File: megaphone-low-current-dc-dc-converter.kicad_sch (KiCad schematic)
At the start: 53 parts, among them Q1 SI7272DP, Q3 2N7002, U2 AP63203WU, U3 ACS712, U4 ACS712, U5 MCP4018

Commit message: change all MPPT references in files to new project name
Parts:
- L1: footprint MPPT Charge Controller Footprint Library:L_Vishay_6.9x6.5 -> megaphone-low-current-dc-dc-converter Footprint Library:L_Vishay_6.9x6.5
- U1: footprint MPPT Charge Controller Footprint Library:VQFN-16_EP_3.5x3.5_Pitch0.5mm -> megaphone-low-current-dc-dc-converter Footprint Library:VQFN-16_EP_3.5x3.5_Pitch0.5mm; symbol MPPT Charge Controller Symbol Library:BQ24650 -> megaphone-low-current-dc-dc-converter Symbol Library:BQ24650
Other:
- title: MEGAphone MPPT Charge Controller -> MEGAphone megaphone-low-current-dc-dc-converter

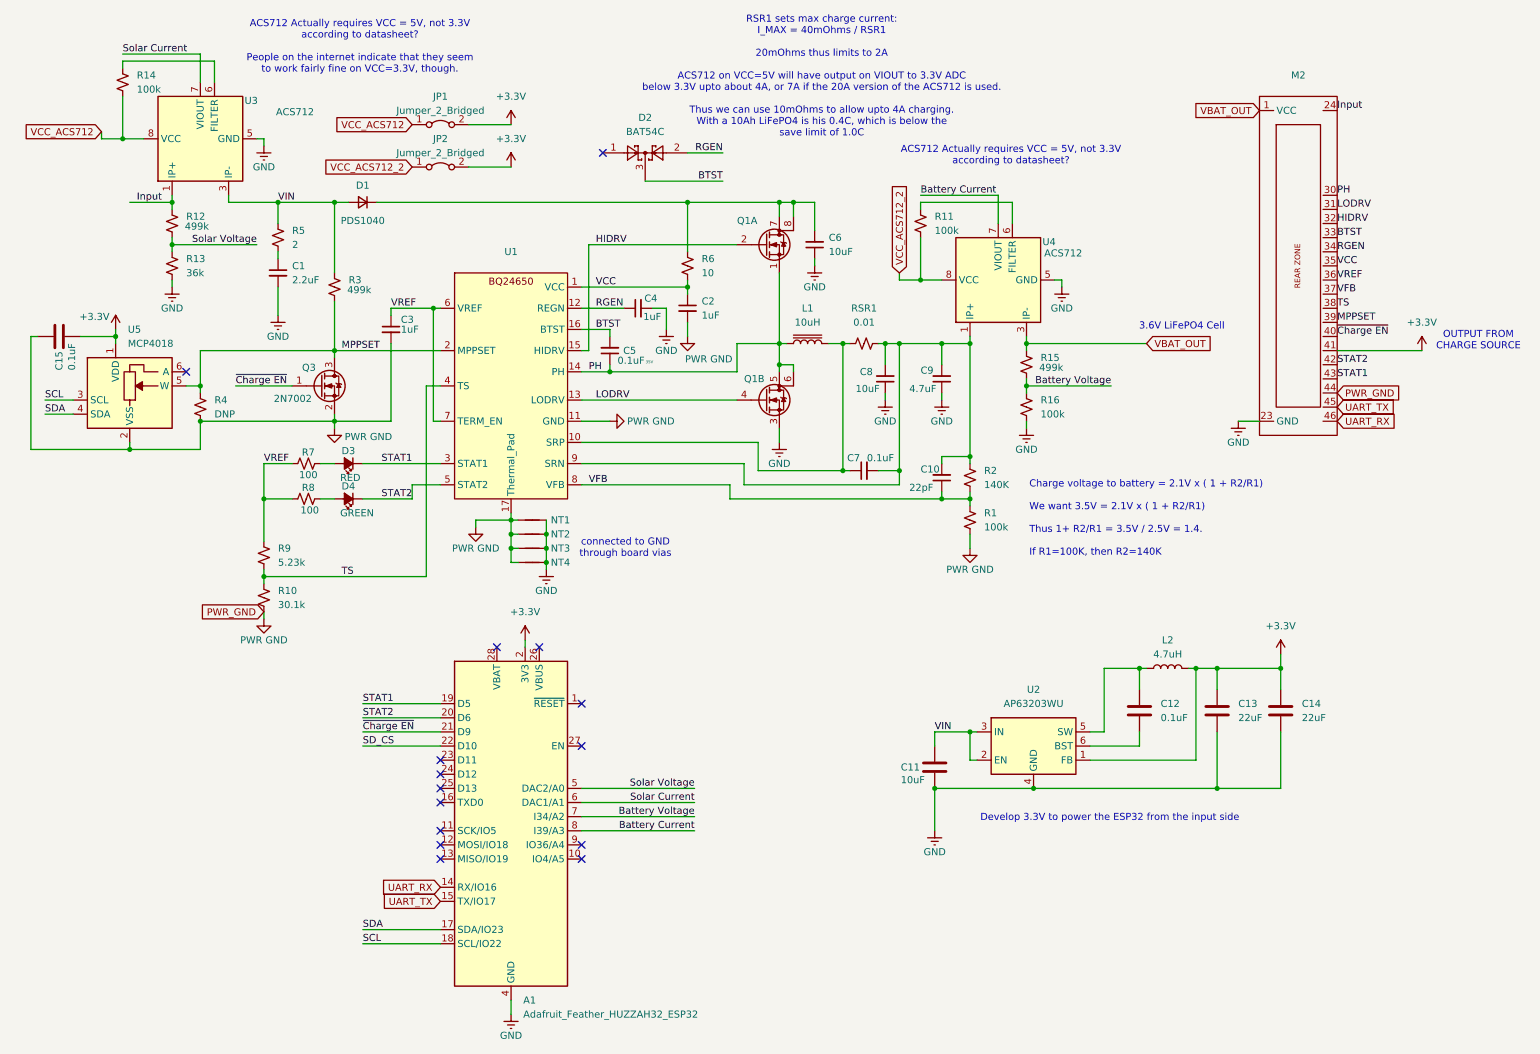
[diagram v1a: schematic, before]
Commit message: prune out unnecessary part of schematic
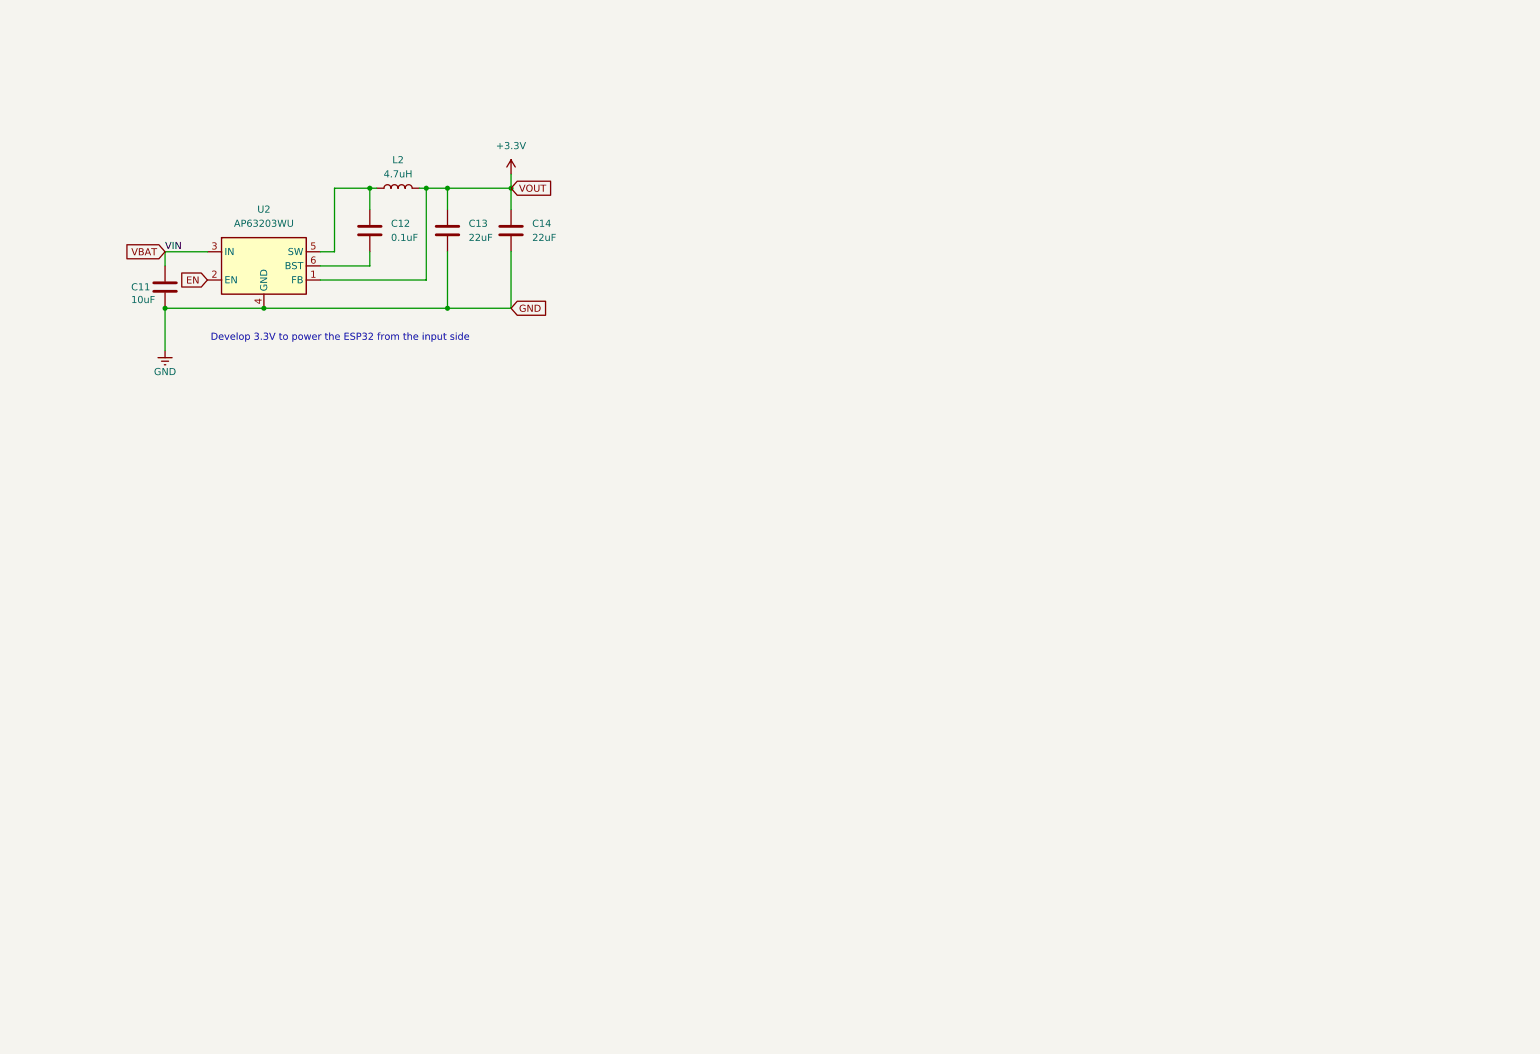
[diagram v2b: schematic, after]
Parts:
- removed A1: Adafruit_Feather_HUZZAH32_ESP32, Module:Adafruit_Feather, symbol MCU_Module:Adafruit_Feather_HUZZAH32_ESP32
- removed C1: 2.2uF, Capacitor_SMD:C_1210_3225Metric, symbol Device:C_Small
- removed C10: 22pF, Capacitor_SMD:C_0603_1608Metric, symbol Device:C_Small
- removed C15: 0.1uF, Capacitor_SMD:C_0603_1608Metric, symbol Device:C
- removed C2, C3, C4: 1uF, Capacitor_SMD:C_0603_1608Metric, symbol Device:C_Small
- removed C5, C7: 0.1uF, Capacitor_SMD:C_0603_1608Metric, symbol Device:C_Small
- removed C6, C8: 10uF, Capacitor_SMD:C_1206_3216Metric, symbol Device:C_Small
- removed C9: 4.7uF, Capacitor_SMD:C_0805_2012Metric, symbol Device:C_Small
- removed D1: PDS1040, Diode_SMD:D_PowerDI-5, symbol Device:D_Small
- removed D2: BAT54C, Package_TO_SOT_SMD:SOT-23, symbol Diode:BAT54C
- removed D3: RED, LED_SMD:LED_0603_1608Metric, symbol Device:LED_Small_Filled
- removed D4: GREEN, LED_SMD:LED_0603_1608Metric, symbol Device:LED_Small_Filled
- removed JP1, JP2: Jumper_2_Bridged, Jumper:SolderJumper-2_P1.3mm_Bridged_RoundedPad1.0x1.5mm, symbol Jumper:Jumper_2_Bridged
- removed L1: 10uH, megaphone-low-current-dc-dc-converter Footprint Library:L_Vishay_6.9x6.5, symbol Device:L_Iron
- removed M2: ~, MegaCastle:MegaCastle2x23-Module-I30.0x53.6-M80000307FFFC-PANEL, symbol MegaCastle:MegaCastle2x23-Module-I30.0x53.6-M80000307FFFC
- removed NT1, NT2, NT3, NT4: ~, NetTie:NetTie-2_SMD_Pad0.5mm, symbol Device:NetTie_2
- removed Q1: SI7272DP, Package_SO:PowerPAK_SO-8_Dual, symbol Device:Q_Dual_NMOS_S1G1S2G2D2D2D1D1
- removed Q3: 2N7002, Package_TO_SOT_SMD:SOT-23, symbol Transistor_FET:2N7002
- removed R1, R11, R14, R16: 100k, Resistor_SMD:R_0603_1608Metric, symbol Device:R_Small_US
- removed R10: 30.1k, Resistor_SMD:R_0603_1608Metric, symbol Device:R_Small_US
- removed R12, R15, R3: 499k, Resistor_SMD:R_0603_1608Metric, symbol Device:R_Small_US
- removed R13: 36k, Resistor_SMD:R_0603_1608Metric, symbol Device:R_Small_US
- removed R2: 140K, Resistor_SMD:R_0603_1608Metric, symbol Device:R_Small_US
- removed R4: DNP, Resistor_SMD:R_0603_1608Metric, symbol Device:R_Small_US
- removed R5: 2, Resistor_SMD:R_2512_6332Metric, symbol Device:R_Small_US
- removed R6: 10, Resistor_SMD:R_0603_1608Metric, symbol Device:R_Small_US
- removed R7, R8: 100, Resistor_SMD:R_0603_1608Metric, symbol Device:R_Small_US
- removed R9: 5.23k, Resistor_SMD:R_0603_1608Metric, symbol Device:R_Small_US
- removed RSR1: 0.01, Resistor_SMD:R_1206_3216Metric, symbol Device:R_Small_US
- removed U1: ~, megaphone-low-current-dc-dc-converter Footprint Library:VQFN-16_EP_3.5x3.5_Pitch0.5mm, symbol megaphone-low-current-dc-dc-converter Symbol Library:BQ24650
- removed U3, U4: ACS712, Package_SO:SOIC-8_3.9x4.9mm_P1.27mm, symbol Sensor_Current:ACS712xLCTR-05B
- removed U5: MCP4018, Package_TO_SOT_SMD:SOT-363_SC-70-6, symbol Potentiometer_Digital:MCP4018-xxxxLT
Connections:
- net VIN renamed VBAT
- net VBAT: no longer U2.2 (EN)
- new net EN: U2.2 (EN)
- no-connect marks 15 -> 0
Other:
- note removed: "3.6V LiFePO4 Cell"
- note removed: "ACS712 Actually requires VCC = 5V, not 3.3V according to datasheet?"
- note removed: "ACS712 Actually requires VCC = 5V, not 3.3V according to datasheet? People on the internet indicate that they seem to work fairly fine on VCC=3.3V, though."
- note removed: "Charge voltage to battery = 2.1V x ( 1 + R2/R1) We want 3.5V = 2.1V x ( 1 + R2/R1) Thus 1+ R2/R1 = 3.5V / 2.5V = 1.4. If R1=100K, then R2=140K"
- note removed: "OUTPUT FROM CHARGE SOURCE"
- note removed: "RSR1 sets max charge current: I_MAX = 40mOhms / RSR1 20mOhms thus limits to 2A ACS712 on VCC=5V will have output on VIOUT to 3.3V ADC below 3.3V upto about 4A, or 7A if the 20A version of the ACS712 is used. Thus we can use 10mOhms to allow upto 4A charging. With a 10Ah LiFePO4 is his 0.4C, which is below the save limit of 1.0C"
- note removed: "connected to GND through board vias"
- moved on the sheet: C11, C12, C13, C14, L2, U2

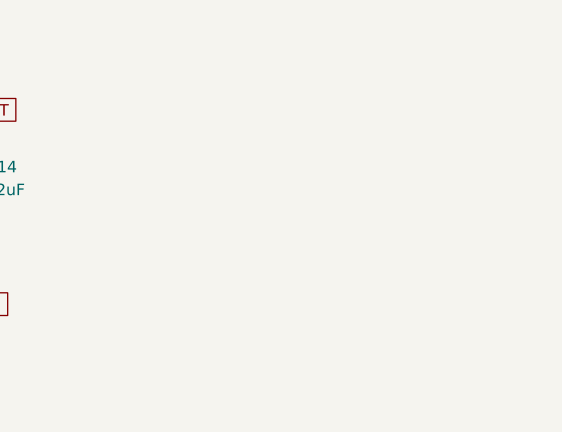
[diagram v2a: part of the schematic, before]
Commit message: finish adapting MPPT into simple low-current 3.3V DC:DC regulator
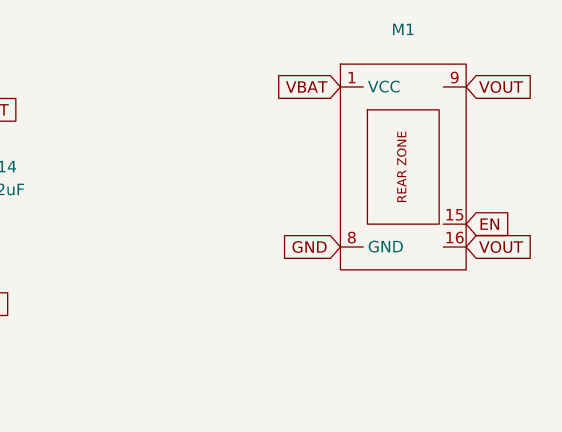
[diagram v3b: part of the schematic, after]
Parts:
- added M1: ~, MegaCastle:MegaCastle2x8-Module-I7.0x15.5-M8183, symbol MegaCastle:MegaCastle2x8-Module-I7.0x15.5-M8183
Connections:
- net +3.3V: now also M1.16, M1.9
- net EN: now also M1.15
- net GND: now also M1.8 (GND)
- net VBAT: now also M1.1 (VCC)
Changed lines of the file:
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@@
+		)
+	)
+	(global_label "VBAT"
+		(shape input)
+		(at 144.78 40.64 180)
+		(fields_autoplaced yes)
+		(effects
+			(font
+				(size 1.27 1.27)
+			)
+			(justify right)
+		)
+		(property "Intersheetrefs" "${INTERSHEET_REFS}"
+			(at 137.38 40.64 0)
+			(effects
+				(font
+					(size 1.27 1.27)
+				)
+				(justify right)
+				(hide yes)
+			)
 		)
 	)
@@
 				)
 				(justify left)
+				(hide yes)
+			)
+		)
+	)
+	(global_label "EN"
+		(shape input)
+		(at 158.75 55.88 0)
+		(fields_autoplaced yes)
+		(effects
+			(font
+				(size 1.27 1.27)
+			)
+			(justify left)
+		)
+		(property "Intersheetrefs" "${INTERSHEET_REFS}"
+			(at 164.2147 55.88 0)
+			(effects
+				(font
+					(size 1.27 1.27)
+				)
+				(justify left)
+				(hide yes)
+			)
+		)
+	)
+	(global_label "VOUT"
+		(shape input)
+		(at 158.75 40.64 0)
+		(fields_autoplaced yes)
+		(effects
+			(font
+				(size 1.27 1.27)
+			)
+			(justify left)
+		)
+		(property "Intersheetrefs" "${INTERSHEET_REFS}"
+			(at 166.4524 40.64 0)
+			(effects
+				(font
+					(size 1.27 1.27)
+				)
+				(justify left)
+				(hide yes)
+			)
+		)
+	)
+	(global_label "VOUT"
+		(shape input)
+		(at 158.75 58.42 0)
+		(fields_autoplaced yes)
+		(effects
+			(font
+				(size 1.27 1.27)
+			)
+			(justify left)
+		)
+		(property "Intersheetrefs" "${INTERSHEET_REFS}"
+			(at 166.4524 58.42 0)
+			(effects
+				(font
+					(size 1.27 1.27)
+				)
+				(justify left)
+				(hide yes)
+			)
+		)
+	)
+	(global_label "GND"
+		(shape input)
+		(at 144.78 58.42 180)
+		(fields_autoplaced yes)
+		(effects
+			(font
+				(size 1.27 1.27)
+			)
+			(justify right)
+		)
+		(property "Intersheetrefs" "${INTERSHEET_REFS}"
+			(at 137.9243 58.42 0)
+			(effects
+				(font
+					(size 1.27 1.27)
+				)
+				(justify right)
 				(hide yes)
 			)
@@
 					(unit 1)
 				)
+			)
+		)
+	)
+	(symbol
+		(lib_id "MegaCastle:MegaCastle2x8-Module-I7.0x15.5-M8183")
+		(at 151.13 49.53 0)
+		(unit 1)
+		(exclude_from_sim no)
+		(in_bom yes)
+		(on_board yes)
+		(dnp no)
+		(fields_autoplaced yes)
+		(property "Reference" "M1"
+			(at 151.765 34.29 0)
+			(effects
+				(font
+					(size 1.27 1.27)
+				)
+			)
+		)
+		(property "Value" "~"
+			(at 151.765 36.83 0)
+			(effects
+				(font
+					(size 1.27 1.27)
+				)
+			)
+		)
+		(property "Footprint" "MegaCastle:MegaCastle2x8-Module-I7.0x15.5-M8183"
+			(at 151.13 66.04 0)
+			(effects
+				(font
+					(size 1.27 1.27)
+				)
+				(hide yes)
+			)
+		)
+		(property "Datasheet" ""
+			(at 151.13 44.45 0)
+			(effects
+				(font
+					(size 1.27 1.27)
+				)
+				(hide yes)
+			)
+		)
+		(property "Description" "Generated using footprint-gen .. 7 14 5 M8183"
+			(at 151.13 49.53 0)
+			(effects
+				(font
+					(size 1.27 1.27)
+				)
+				(hide yes)
+			)
+		)
+		(pin "1"
+		)
+		(pin "8"
+		)
+		(pin "9"
+		)
+		(pin "16"
+		)
+		(pin "15"
+		)
+		(instances
+			(project ""
+				(path "/6fccb5b0-46ff-4014-9169-aa61e4064f3f"
+					(reference "M1")
+					(unit 1)
+				)
